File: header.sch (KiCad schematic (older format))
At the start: 21 parts, among them J1 Conn_01x10, J2 Conn_01x08, J3 Conn_01x06, J4 Conn_01x08, SW6 SW_Push, U1 ICE40HX4K-TQ144, U8 TXS0108EPW, U9 TXS0108EPW

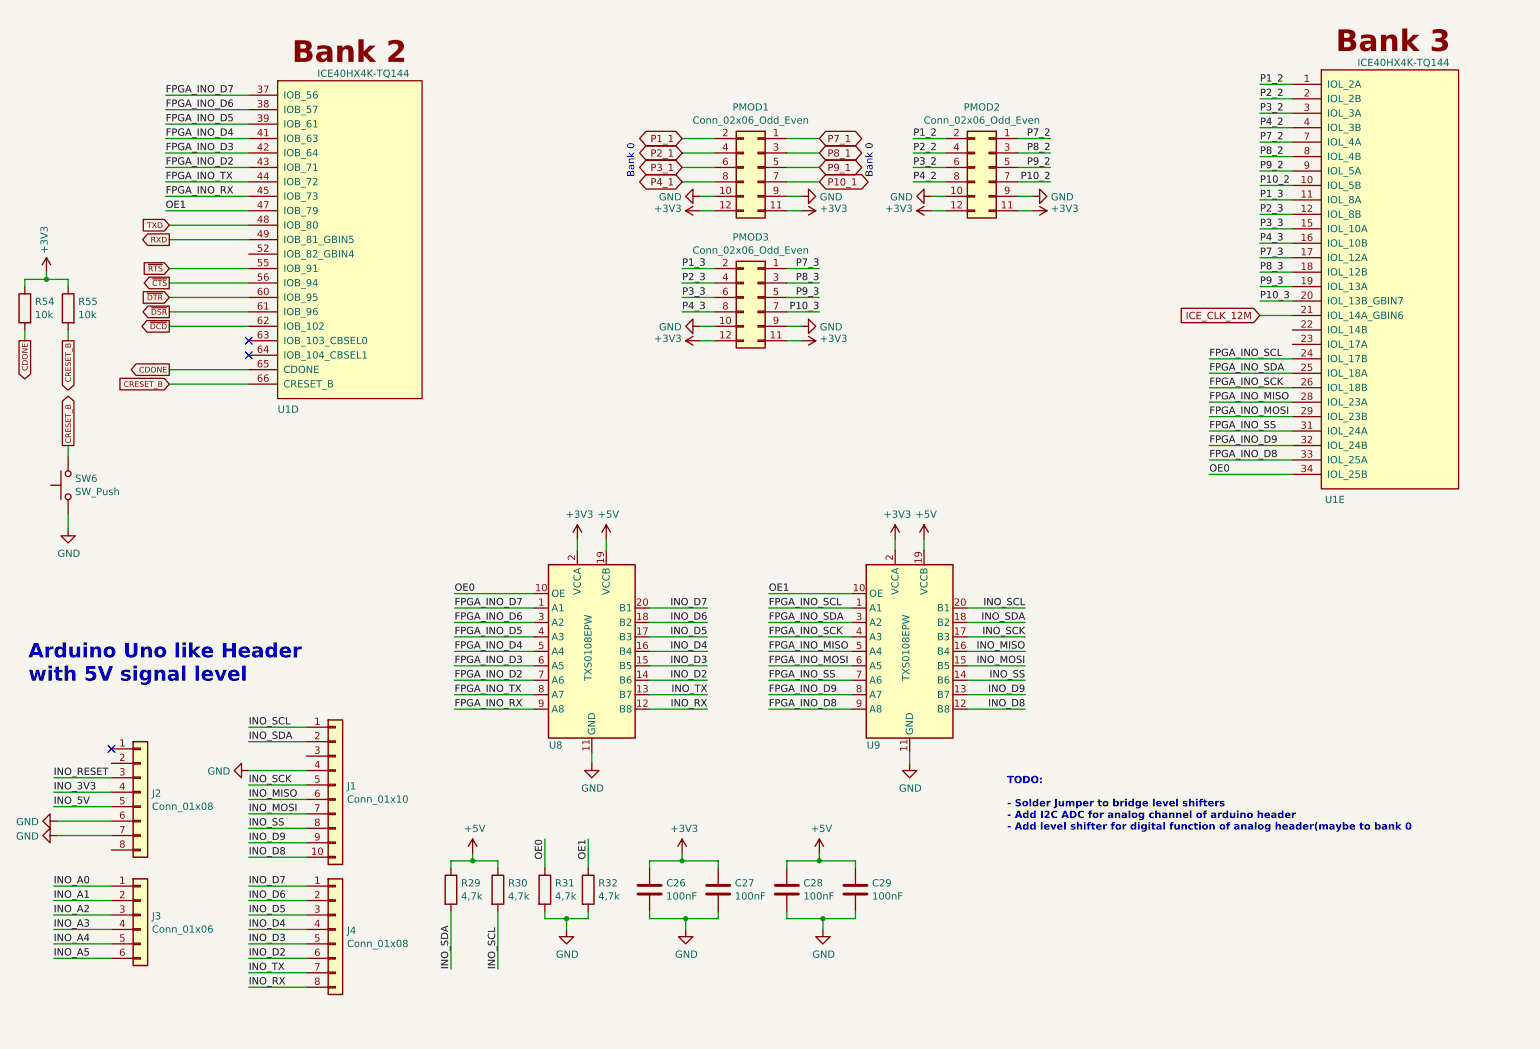
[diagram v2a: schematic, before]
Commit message: Added switches, added 5 V rail and 17 V input(with filtering). Power is mostly done.
Also added a first version of buffers to ftdi chip. I'll change the evtl.

Started to route power section.
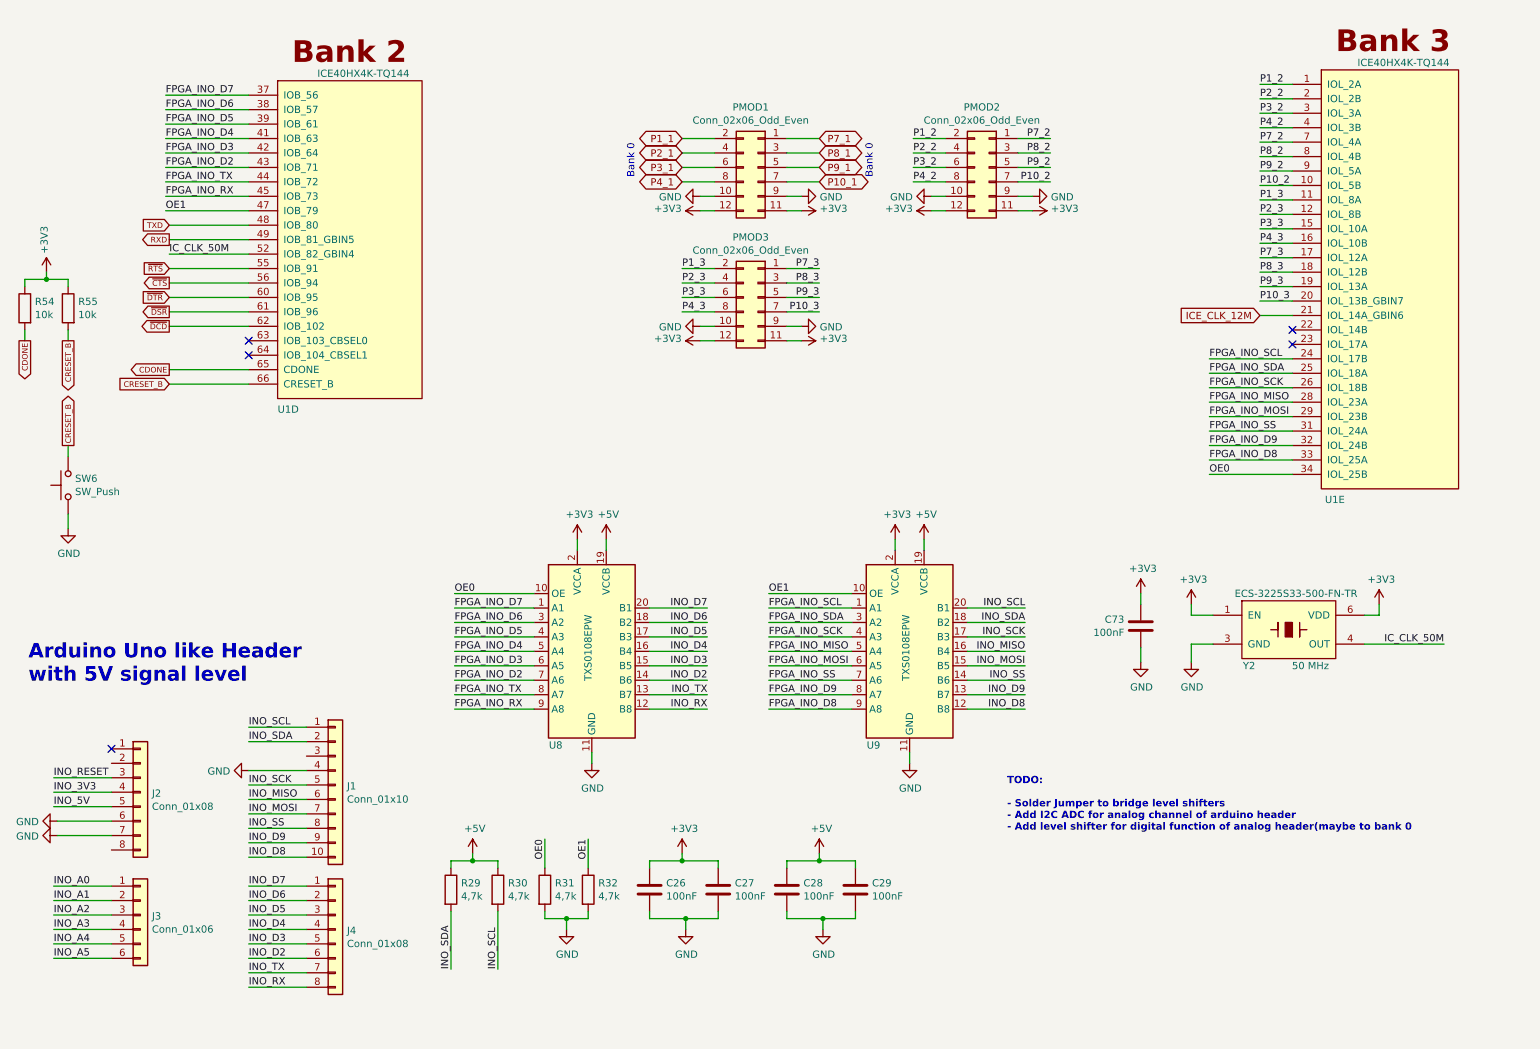
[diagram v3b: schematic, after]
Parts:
- added C73: 100nF, Capacitor_SMD:C_0603_1608Metric, symbol Device:C
- added Y2: ECS-3225S33-500-FN-TR, footprints:ECS-3225S_3.2x2.5mm_footprint, symbol ECS-3225S:ECS-3225S33
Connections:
- net +3V3: now also C73.1, Y2.1 (EN), Y2.6 (VDD)
- net GND: now also C73.2, Y2.3 (GND)
- net IC_CLK_50M: now reaches U1.52 (IOB_82_GBIN4)
- net IC_CLK_50M: now also Y2.4 (OUT)
- no-connect marks 3 -> 5
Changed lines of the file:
@@
 	1    0    0    -1
 $EndComp
+$Comp
+L ECS-3225S:ECS-3225S33 Y?
+U 1 1 5E36217B
+P 9550 4800
+AR Path="/5CAB8B22/5E36217B" Ref="Y?"  Part="1"
+AR Path="/5CB5889B/5E36217B" Ref="Y2"  Part="1"
+F 0 "Y2" H 9250 4550 50  0000 C CNN
+F 1 "ECS-3225S33-500-FN-TR" H 9575 5050 50  0000 C CNN
+F 2 "footprints:ECS-3225S_3.2x2.5mm_footprint" H 9550 4200 50  0001 C CNN
+F 3 "https://www.ecsxtal.com/store/pdf/ECS-3225S.pdf" H 9550 4200 50  0001 C CNN
+F 4 "ECS Inc." H 9550 4800 50  0001 C CNN "Mfg Name"
+F 5 "ECS-3225S33-500-FN-TR" H 9550 4800 50  0001 C CNN "Mfg Part Num"
+F 6 "XC2226CT-ND" H 9550 4800 50  0001 C CNN "Digikey"
+F 7 "XTAL OSC XO 50.0000MHZ HCMOS SMD" H 9550 4800 50  0001 C CNN "Description"
+F 8 "50 MHz" H 9675 4550 50  0000 C CNN "f"
+	1    9550 4800
+	1    0    0    -1
+$EndComp
+Wire Wire Line
+	10050 4700 10150 4700
+Wire Wire Line
+	10150 4700 10150 4625
+$Comp
+L power:GND #PWR?
+U 1 1 5E362183
+P 8850 5025
+AR Path="/5CAB8B22/5E362183" Ref="#PWR?"  Part="1"
+AR Path="/5CB5889B/5E362183" Ref="#PWR0161"  Part="1"
+F 0 "#PWR0161" H 8850 4775 50  0001 C CNN
+F 1 "GND" H 8855 4852 50  0000 C CNN
+F 2 "" H 8850 5025 50  0001 C CNN
+F 3 "" H 8850 5025 50  0001 C CNN
+	1    8850 5025
+	1    0    0    -1
+$EndComp
+Wire Wire Line
+	8850 5025 8850 4900
+Wire Wire Line
+	8850 4900 9000 4900
+$Comp
+L power:GND #PWR?
+U 1 1 5E36218B
+P 8500 5025
+AR Path="/5CAB8B22/5E36218B" Ref="#PWR?"  Part="1"
+AR Path="/5CB5889B/5E36218B" Ref="#PWR0162"  Part="1"
+F 0 "#PWR0162" H 8500 4775 50  0001 C CNN
+F 1 "GND" H 8505 4852 50  0000 C CNN
+F 2 "" H 8500 5025 50  0001 C CNN
+F 3 "" H 8500 5025 50  0001 C CNN
+	1    8500 5025
+	1    0    0    -1
+$EndComp
+Wire Wire Line
+	8500 5025 8500 4925
+Wire Wire Line
+	8500 4550 8500 4625
+Wire Wire Line
+	10050 4900 10600 4900
+Wire Wire Line
+	8850 4625 8850 4700
+Wire Wire Line
+	8850 4700 9000 4700
+$Comp
+L Device:C C?
+U 1 1 5E3621A8
+P 8500 4775
+AR Path="/5CAB7CD4/5E3621A8" Ref="C?"  Part="1"
+AR Path="/5CAB8B22/5E3621A8" Ref="C?"  Part="1"
+AR Path="/5CB5889B/5E3621A8" Ref="C73"  Part="1"
+F 0 "C73" H 8386 4821 50  0000 R CNN
+F 1 "100nF" H 8386 4730 50  0000 R CNN
+F 2 "Capacitor_SMD:C_0603_1608Metric" H 8538 4625 50  0001 C CNN
+F 3 "~" H 8500 4775 50  0001 C CNN
+	1    8500 4775
+	1    0    0    -1
+$EndComp
+$Comp
+L power:+3V3 #PWR0163
+U 1 1 5E36F542
+P 8500 4550
+F 0 "#PWR0163" H 8500 4400 50  0001 C CNN
+F 1 "+3V3" H 8515 4723 50  0000 C CNN
+F 2 "" H 8500 4550 50  0001 C CNN
+F 3 "" H 8500 4550 50  0001 C CNN
+	1    8500 4550
+	1    0    0    -1
+$EndComp
+$Comp
+L power:+3V3 #PWR0164
+U 1 1 5E36FE40
+P 8850 4625
+F 0 "#PWR0164" H 8850 4475 50  0001 C CNN
+F 1 "+3V3" H 8865 4798 50  0000 C CNN
+F 2 "" H 8850 4625 50  0001 C CNN
+F 3 "" H 8850 4625 50  0001 C CNN
+	1    8850 4625
+	1    0    0    -1
+$EndComp
+$Comp
+L power:+3V3 #PWR0165
+U 1 1 5E3701D9
+P 10150 4625
+F 0 "#PWR0165" H 10150 4475 50  0001 C CNN
+F 1 "+3V3" H 10165 4798 50  0000 C CNN
+F 2 "" H 10150 4625 50  0001 C CNN
+F 3 "" H 10150 4625 50  0001 C CNN
+	1    10150 4625
+	1    0    0    -1
+$EndComp
+Text Label 10600 4900 2    50   ~ 0
+IC_CLK_50M
+Text Label 1775 2200 0    50   ~ 0
+IC_CLK_50M
+Wire Wire Line
+	1775 2200 2325 2200
+NoConn ~ 9550 2725
+NoConn ~ 9550 2825
 $EndSCHEMATC

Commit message: Continued with routing
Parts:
- added D17: DONE, LED_SMD:LED_0603_1608Metric, symbol Device:LED_ALT
- added Q2: Q_NMOS_GSD, Package_TO_SOT_SMD:SOT-23, symbol Device:Q_NMOS_GSD
- added R60: 560, Resistor_SMD:R_0603_1608Metric, symbol Device:R
- added U?: MAX11615, Package_SO:QSOP-16_3.9x4.9mm_P0.635mm, symbol Analog_ADC:MAX11615
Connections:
- net +3V3: now also R60.1
- net CDONE: now also Q2.1 (G)
- net GND: now also Q2.2 (S)
- net INO_A0: now also U?.5 (AIN0)
- net INO_A1: now also U?.6 (AIN1)
- net INO_A2: now also U?.7 (AIN2)
- net INO_A3: now also U?.8 (AIN3)
- net INO_A4: now also U?.9 (AIN4)
- net INO_A5: now also U?.10 (AIN5)
- new net: D17.1 (K), Q2.3 (D)
- new net: D17.2 (A), R60.2
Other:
- note removed: "TODO:\n\n- Solder Jumper to bridge level shifters\n- Add I2C ADC for analog channel of arduino header\n- Add level shifter for digital function of analog header(maybe to bank 0"
- moved on the sheet: C73, U1E, Y2

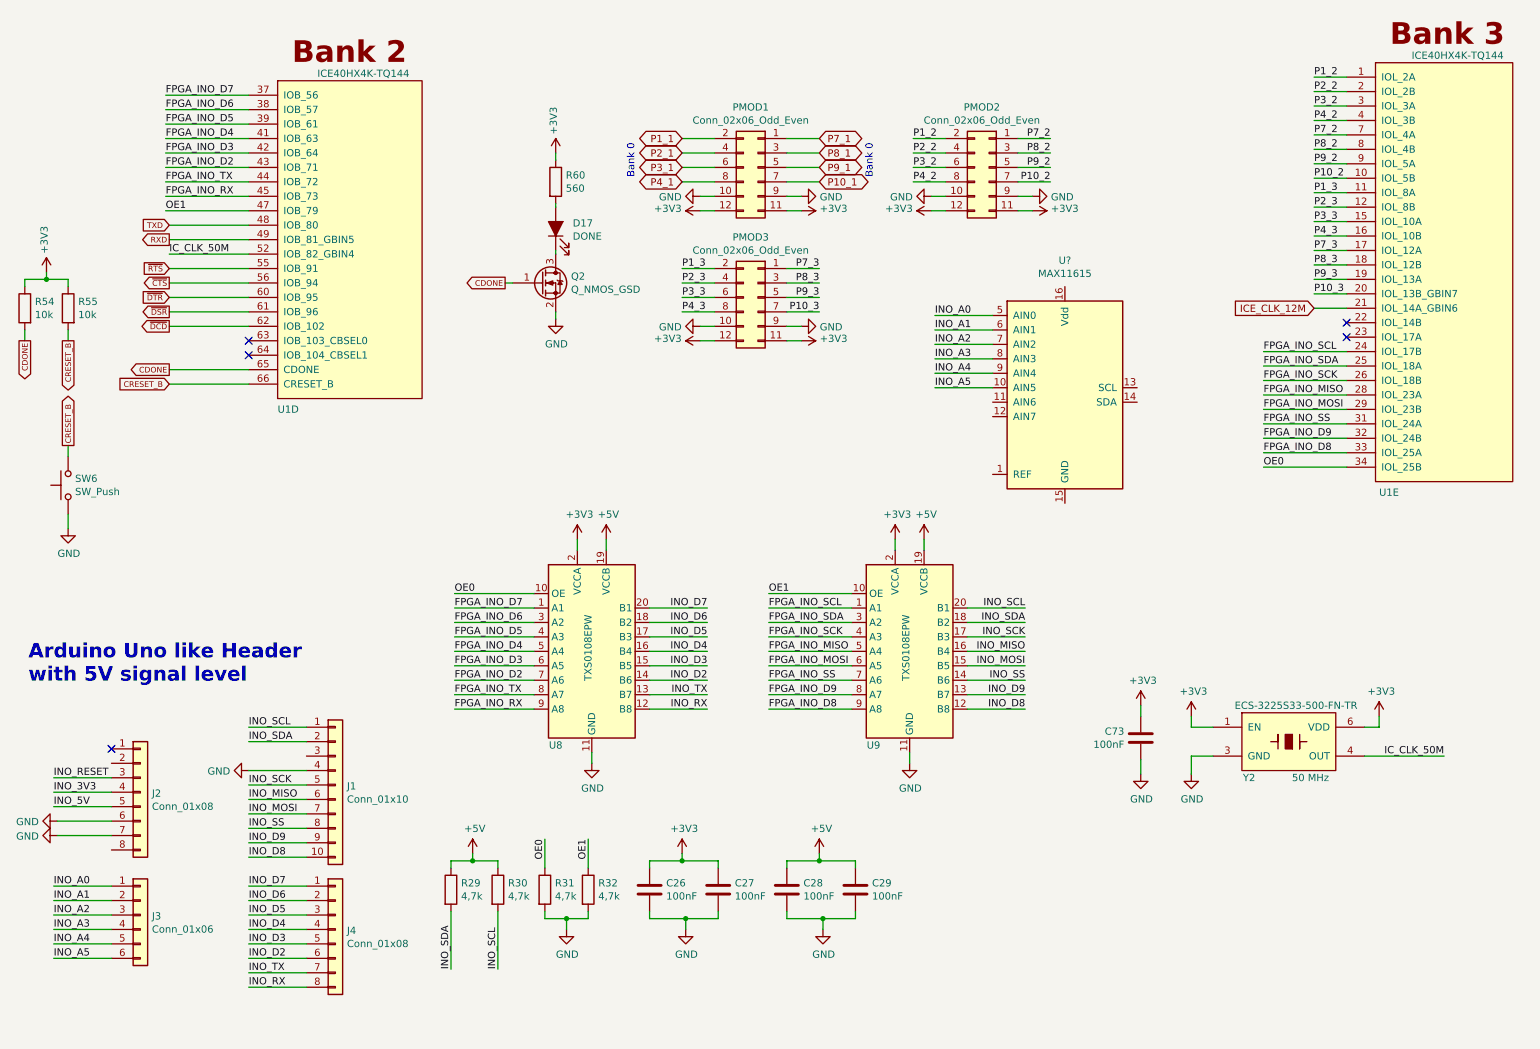
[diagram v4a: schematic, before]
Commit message: Continued with routing and added ADC
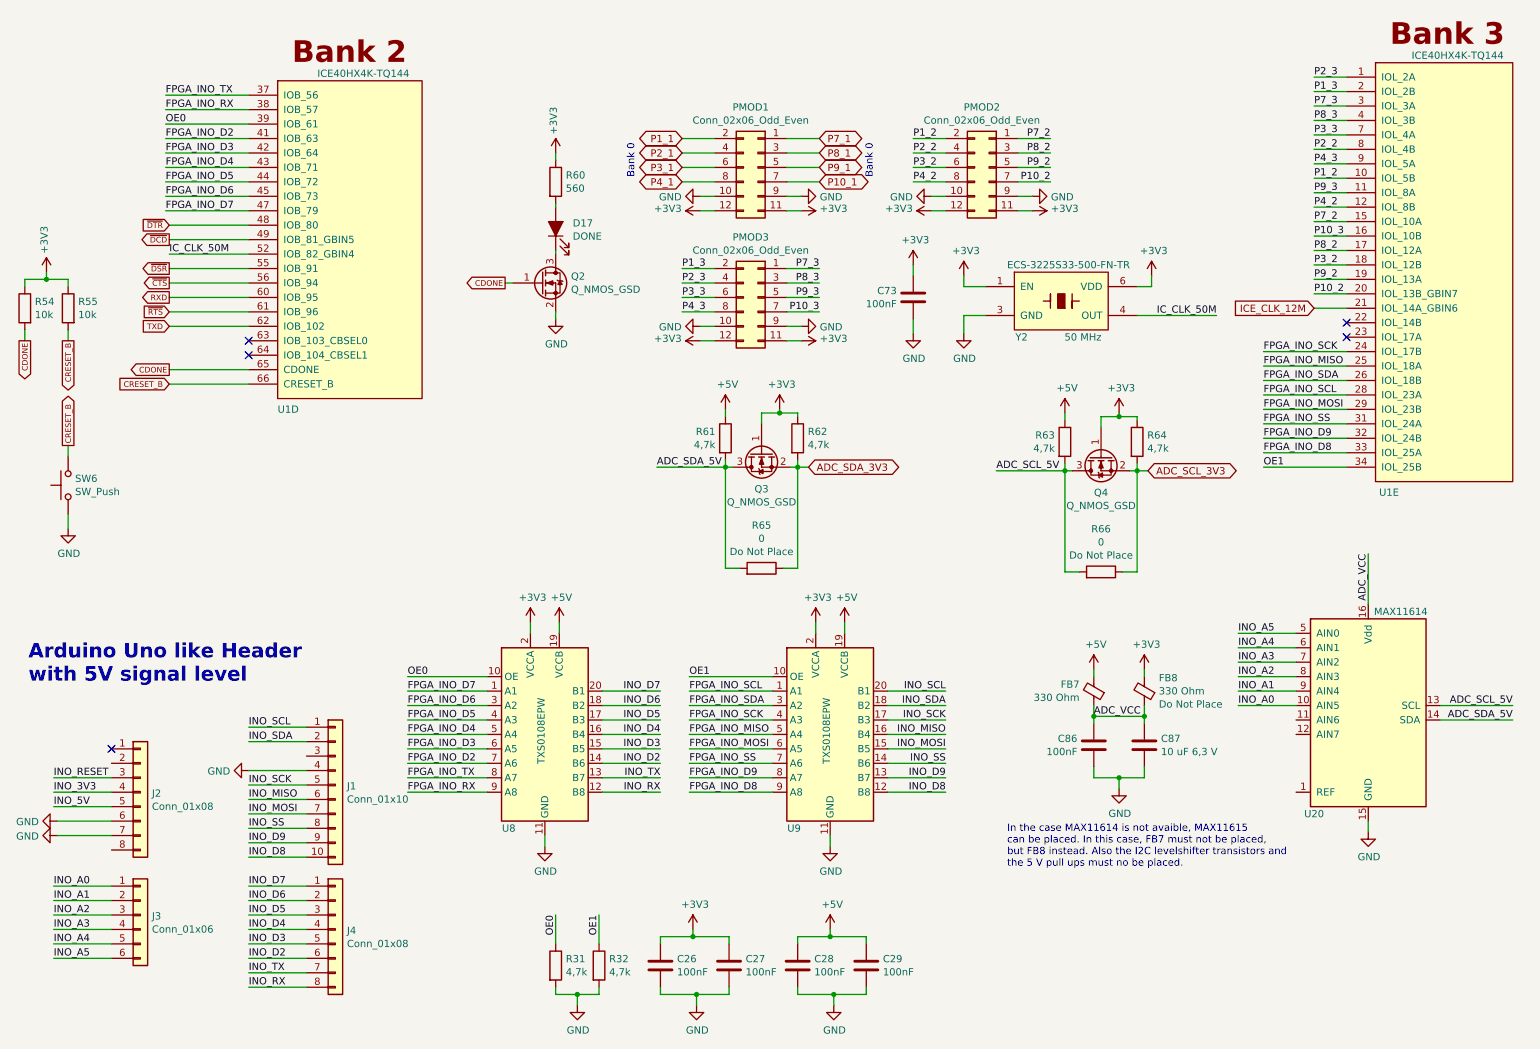
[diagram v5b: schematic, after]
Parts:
- removed R29, R30: 4,7k, Resistor_SMD:R_0603_1608Metric, symbol Device:R
- removed U?: MAX11615, Package_SO:QSOP-16_3.9x4.9mm_P0.635mm, symbol Analog_ADC:MAX11615
- added C86: 100nF, Capacitor_SMD:C_0603_1608Metric, symbol Device:C
- added C87: 10 uF 6,3 V, Capacitor_SMD:C_0603_1608Metric, symbol Device:C
- added FB7, FB8: 330 Ohm, Resistor_SMD:R_0805_2012Metric, symbol Device:Ferrite_Bead_Small
- added Q3, Q4: Q_NMOS_GSD, Package_TO_SOT_SMD:SOT-23, symbol Device:Q_NMOS_GSD
- added R61, R62, R63, R64: 4,7k, Resistor_SMD:R_0603_1608Metric, symbol Device:R
- added R65, R66: 0, Resistor_SMD:R_0603_1608Metric, symbol Device:R
- added U20: MAX11614, Package_SO:QSOP-16_3.9x4.9mm_P0.635mm, symbol Analog_ADC:MAX11614
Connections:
- net +3V3: now also FB8.2, Q3.1 (G), Q4.1 (G), R62.1, R64.1
- net +5V: now also FB7.2, R61.1, R63.1
- net FPGA_INO_D2: now also U1.41 (IOB_63); no longer U1.43 (IOB_71)
- net FPGA_INO_D4: now also U1.43 (IOB_71); no longer U1.41 (IOB_63)
- net FPGA_INO_D5: now also U1.44 (IOB_72); no longer U1.39 (IOB_61)
- net FPGA_INO_D6: now also U1.45 (IOB_73); no longer U1.38 (IOB_57)
- net FPGA_INO_D7: now also U1.47 (IOB_79); no longer U1.37 (IOB_56)
- net FPGA_INO_MISO: now also U1.25 (IOL_18A); no longer U1.28 (IOL_23A)
- net FPGA_INO_RX: now also U1.38 (IOB_57); no longer U1.45 (IOB_73)
- net FPGA_INO_SCK: now also U1.24 (IOL_17B); no longer U1.26 (IOL_18B)
- net FPGA_INO_SCL: now also U1.28 (IOL_23A); no longer U1.24 (IOL_17B)
- net FPGA_INO_SDA: now also U1.26 (IOL_18B); no longer U1.25 (IOL_18A)
- net FPGA_INO_TX: now also U1.37 (IOB_56); no longer U1.44 (IOB_72)
- net GND: now also C86.2, C87.2, U20.15 (GND)
- net INO_A0: now also U20.10 (AIN5)
- net INO_A1: now also U20.9 (AIN4)
- net INO_A2: now also U20.8 (AIN3)
- net INO_A3: now also U20.7 (AIN2)
- net INO_A4: now also U20.6 (AIN1)
- net INO_A5: now also U20.5 (AIN0)
- net OE0: now also U1.39 (IOB_61); no longer U1.34 (IOL_25B)
- net OE1: now also U1.34 (IOL_25B); no longer U1.47 (IOB_79)
- net P10_2: now also U1.20 (IOL_13B_GBIN7); no longer U1.10 (IOL_5B)
- net P10_3: now also U1.16 (IOL_10B); no longer U1.20 (IOL_13B_GBIN7)
- net P1_2: now also U1.10 (IOL_5B); no longer U1.1 (IOL_2A)
- net P1_3: now also U1.2 (IOL_2B); no longer U1.11 (IOL_8A)
- net P2_2: now also U1.8 (IOL_4B); no longer U1.2 (IOL_2B)
- net P2_3: now also U1.1 (IOL_2A); no longer U1.12 (IOL_8B)
- net P3_2: now also U1.18 (IOL_12B); no longer U1.3 (IOL_3A)
- net P3_3: now also U1.7 (IOL_4A); no longer U1.15 (IOL_10A)
- net P4_2: now also U1.12 (IOL_8B); no longer U1.4 (IOL_3B)
- net P4_3: now also U1.9 (IOL_5A); no longer U1.16 (IOL_10B)
- net P7_2: now also U1.15 (IOL_10A); no longer U1.7 (IOL_4A)
- net P7_3: now also U1.3 (IOL_3A); no longer U1.17 (IOL_12A)
- net P8_2: now also U1.17 (IOL_12A); no longer U1.8 (IOL_4B)
- net P8_3: now also U1.4 (IOL_3B); no longer U1.18 (IOL_12B)
- net P9_2: now also U1.19 (IOL_13A); no longer U1.9 (IOL_5A)
- net P9_3: now also U1.11 (IOL_8A); no longer U1.19 (IOL_13A)
- net RXD: now also U1.60 (IOB_95); no longer U1.49 (IOB_81_GBIN5)
- net TXD: now also U1.62 (IOB_102); no longer U1.48 (IOB_80)
- net ~DCD~: now also U1.49 (IOB_81_GBIN5); no longer U1.62 (IOB_102)
- net ~DSR~: now also U1.55 (IOB_91); no longer U1.61 (IOB_96)
- net ~DTR~: now also U1.48 (IOB_80); no longer U1.60 (IOB_95)
- net ~RTS~: now also U1.61 (IOB_96); no longer U1.55 (IOB_91)
- new net ADC_SCL_3V3: Q4.2 (S), R64.2, R66.1
- new net ADC_SCL_5V: Q4.3 (D), R63.2, R66.2, U20.13 (SCL)
- new net ADC_SDA_3V3: Q3.2 (S), R62.2, R65.1
- new net ADC_SDA_5V: Q3.3 (D), R61.2, R65.2, U20.14 (SDA)
- new net ADC_VCC: C86.1, C87.1, FB7.1, FB8.1, U20.16 (Vdd)
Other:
- note added: "In the case MAX11614 is not avaible, MAX11615\ncan be placed. In this case, FB7 must not be placed,\nbut FB8 instead. Also the I2C levelshifter transistors and\nthe 5 V pull ups must no be placed."
- moved on the sheet: C26, C27, C28, C29, C73, R31, R32, U8, U9, Y2
